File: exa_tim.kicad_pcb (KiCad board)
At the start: 4 copper layers, 42 x 42 mm, 54 parts, among them J1 20021121-00010C4LF, J2 FH12-24S-0.5SH(55), Q1 SI2333DS-T1-E3, Q2 DMN3067LW-7, SW1 SKRTLBE010, SW2 SKRTLBE010, SW3 SKRTLBE010, SW4 SKRTLBE010, U1 STM32L071KZUx, U2 CAM-M8C-0, Y1 9HT11-32.768KDZF-T

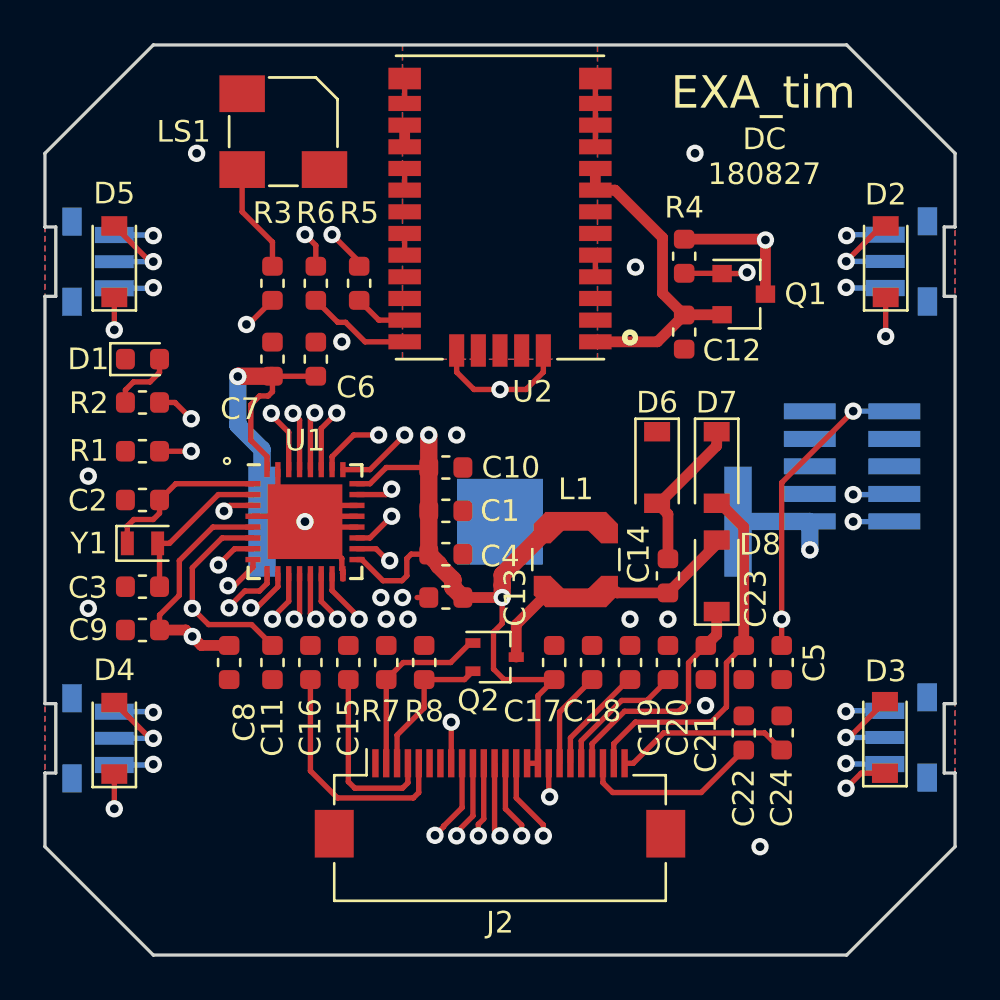
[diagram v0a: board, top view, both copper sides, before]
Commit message: Revert PCB cutout and change button layout
Buttons are not top facing for easier assembly.
First inner layer is now power lane.
Removed useless LED, since we have no way to illuminate
the epaper display.
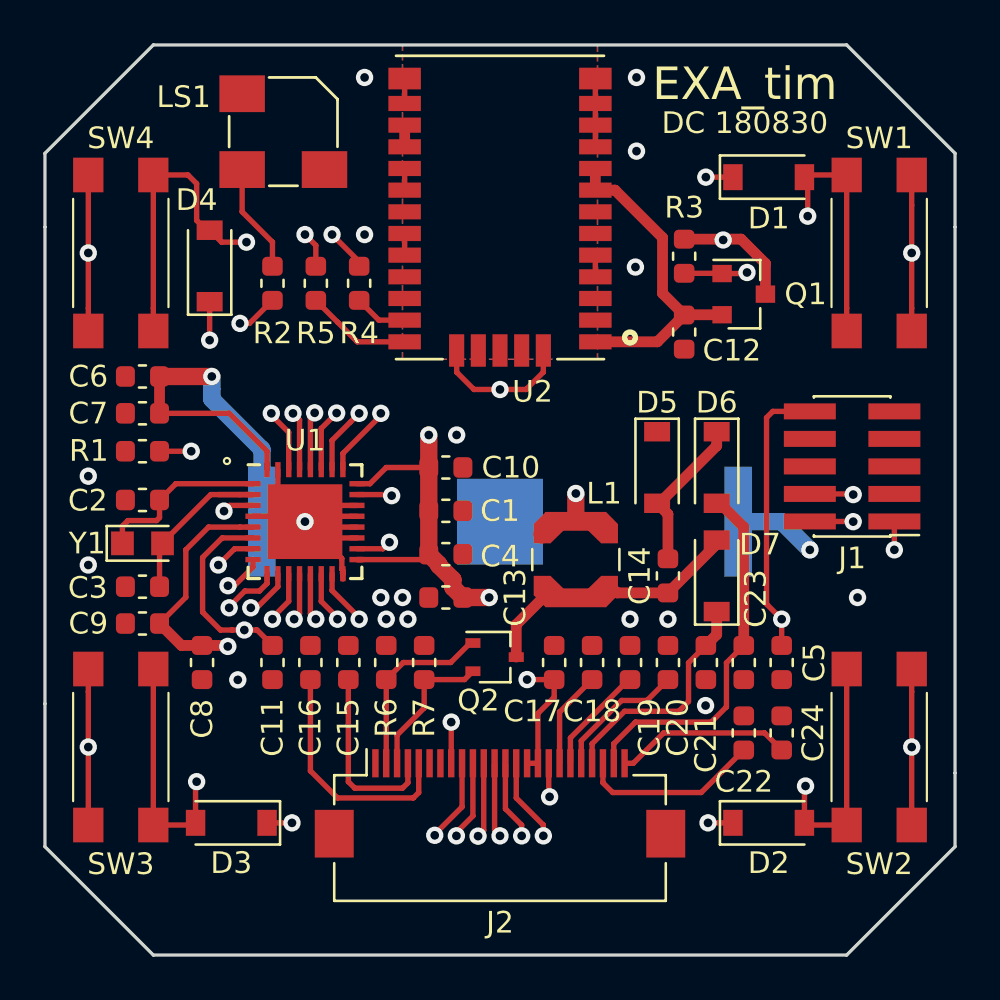
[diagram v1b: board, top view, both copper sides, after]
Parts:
- removed the D1 at (104.5, 84.5)
- removed the D4 at (103.2, 102.0)
- removed the R2 at (104.5, 86.5)
- added D3: MBR0530, Diode_SMD:D_SOD-123, F.Cu at (108.6, 105.9)
- J1: moved to F.Cu
- SW1, SW2, SW3, SW4: value SKRTLBE010 -> TL3305CF260QG; footprint exa_tim:SKRTLBE010 -> exa_tim:TL3305; moved to F.Cu
- Y1: footprint Crystal:Crystal_SMD_TXC_9HT11-2Pin_2.0x1.2mm -> exa_tim:Crystal_SMD_TXC_9HT11-2Pin_2.0x1.2mm_HandSoldering
- moved C6 8.04 mm to (104.5, 85.3), turned to 0 degrees
- moved D1 6.66 mm to (133.4, 76.1), turned to 0 degrees
- moved D2 6.66 mm to (133.4, 105.9), turned to 0 degrees
- moved C7 6.50 mm to (104.5, 87.0), turned to 0 degrees
- moved D4 4.40 mm to (107.6, 80.2)
- moved SW3 1.26 mm to (103.5, 102.4), turned to 270 degrees
- moved SW4 1.26 mm to (103.5, 79.6), turned to 270 degrees
- moved C8 1.25 mm to (107.2, 98.5)
- moved SW2 1.25 mm to (138.5, 102.4), turned to 90 degrees
- moved SW1 1.24 mm to (138.5, 79.6), turned to 90 degrees
- moved C9 0.30 mm to (104.5, 96.7)
- turned J1 to 180 degrees
- renumbered D2 to D1, D3 to D2, D5 to D4, D6 to D5, D7 to D6, D8 to D7, R3 to R2, R4 to R3, R5 to R4, R6 to R5, R7 to R6, R8 to R7
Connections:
- U1 pad 12: /CS -> /BUSY
- U1 pad 18: /BUSY -> /CS
- U1 pad 19: /LED -> GND
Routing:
- net 3V: track 218.7 -> 97.8 mm, vias 14 -> 13
- net /LED: track 14.9 -> 0.00 mm, vias 2 -> 0
- net /WKUP1: track 101.5 -> 114.8 mm
- net /BTN4: track 16.7 -> 25.3 mm
- net /BTN2: track 40.6 -> 48.9 mm
- net /CS: track 27.6 -> 20.7 mm
- net /BTN1: track 34.5 -> 41.3 mm
- net /BUSY: track 19.1 -> 24.7 mm
- net /BTN3: track 32.0 -> 35.1 mm
- net Net-(D1-Pad2): track 3.10 -> 0.00 mm
- net GND: track 35.6 -> 37.8 mm, vias 18 -> 20
- net Net-(C3-Pad1): track 7.37 -> 9.45 mm
- net /SWCLK: track 27.1 -> 28.7 mm
- net /ALARM: track 16.9 -> 18.5 mm
- net /RX: track 29.9 -> 31.2 mm
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- added copper zone on In1.Cu, net 3V
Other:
- outline, holes or cut-outs redrawn
- board text added: "DC 180830"
- board text removed: "DC 180827"

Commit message: Chang Cortex Debug header to right angle TH
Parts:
- J1: value 20021121-00010C4LF -> 20021112-00010T4LF; footprint exa_tim:PinHeader_2x05_P1.27mm_Vertical_SMD -> Connector_PinHeader_1.27mm:PinHeader_2x06_P1.27mm_Horizontal
- moved J1 2.84 mm to (134.7, 88.2), turned to 0 degrees
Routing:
- net /NRST: track 44.2 -> 38.2 mm
- net /SWDIO: track 27.7 -> 23.9 mm, vias 3 -> 2
- net /BTN2: track 48.9 -> 47.9 mm
- net 3V: track 97.8 -> 98.7 mm, vias 13 -> 11
- net /SWCLK: track 28.7 -> 28.4 mm, vias 2 -> 1
- net GND: vias 20 -> 19
